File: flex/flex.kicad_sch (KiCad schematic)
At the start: 139 parts, among them J1 NA_Conn_01x06_Female, J2 NA_Conn_01x05_Female, J3 NA_Conn_01x06_Female, J4 NA_Conn_01x03_Female, J5 NA_Conn_01x03_Female, SW1 SW_Push, SW10 SW_Push, SW11 SW_Push, SW12 SW_Push, SW13 SW_Push, SW14 SW_Push, SW15 SW_Push, SW16 SW_Push, SW17 SW_Push, SW18 SW_Push, SW19 SW_Push, SW2 SW_Push, SW20 SW_Push, SW21 SW_Push, SW22 SW_Push, SW23 SW_Push, SW24 SW_Push, SW3 SW_Push, SW4 SW_Push, SW5 SW_Push, SW6 SW_Push, SW7 SW_Push, SW8 SW_Push, SW9 SW_Push

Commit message: BOM
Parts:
- added C4, C5: C, libs:C_0603_1608Metric, symbol Device:C
- added R4, R5: R, libs:R_0603_1608Metric, symbol Device:R
- C3, J1, J2, J3, J4, J5, Mousebite1, Mousebite10, Mousebite11, Mousebite12, Mousebite2, Mousebite3, Mousebite4, Mousebite5, Mousebite6, Mousebite7, Mousebite8, Mousebite9, R3, SW1, SW10, SW11, SW12, SW13, SW14, SW15, SW16, SW17, SW18, SW19, SW2, SW20, SW21, SW22, SW23, SW24, SW3, SW4, SW5, SW6, SW7, SW8, SW9: now not fitted
- D1, D10, D11, D12, D2, D25, D26, D27, D28, D29, D3, D30, D31, D32, D33, D34, D35, D36, D4, D49, D5, D50, D51, D52, D53, D54, D55, D56, D57, D58, D59, D6, D60, D61, D62, D63, D64, D65, D66, D67, D68, D69, D7, D70, D71, D72, D8, D9: LCSC (none) -> C81598
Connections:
- net Din: now also R4.1, R5.1
- net Gnd: now also C4.2, C5.2
- net Vcc: now also C4.1, C5.1
- net at D13.3 (DIN), D97.3 (DIN), R3.2: now also R4.2, R5.2

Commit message: BOM
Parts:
- D100, D101, D102, D103, D104, D105, D106, D107, D108, D109, D110, D111, D112, D113, D114, D115, D116, D117, D118, D119, D120, D13, D14, D15, D16, D17, D18, D19, D20, D21, D22, D23, D24, D37, D38, D39, D40, D41, D42, D43, D44, D45, D46, D47, D48, D97, D98, D99: LCSC C2890035 -> C5149201
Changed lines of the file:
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@@
 			)
 		)
-		(property "LCSC" "C2890035"
+		(property "LCSC" "C5149201"
 			(at 148.59 204.47 0)
 			(effects
@@
 			)
 		)
-		(property "LCSC" "C2890035"
+		(property "LCSC" "C5149201"
 			(at 193.04 204.47 0)
 			(effects
@@
 			)
 		)
-		(property "LCSC" "C2890035"
+		(property "LCSC" "C5149201"
 			(at 267.97 127 0)
 			(effects
@@
 			)
 		)
-		(property "LCSC" "C2890035"
+		(property "LCSC" "C5149201"
 			(at 148.59 186.69 0)
 			(effects
@@
 			)
 		)
-		(property "LCSC" "C2890035"
+		(property "LCSC" "C5149201"
 			(at 81.28 127 0)
 			(effects
@@
 			)
 		)
-		(property "LCSC" "C2890035"
+		(property "LCSC" "C5149201"
 			(at 312.42 127 0)
 			(effects
@@
 			)
 		)
-		(property "LCSC" "C2890035"
+		(property "LCSC" "C5149201"
 			(at 289.56 146.05 0)
 			(effects
@@
 			)
 		)
-		(property "LCSC" "C2890035"
+		(property "LCSC" "C5149201"
 			(at 223.52 127 0)
 			(effects
@@
 			)
 		)
-		(property "LCSC" "C2890035"
+		(property "LCSC" "C5149201"
 			(at 82.55 186.69 0)
 			(effects
@@
 			)
 		)
-		(property "LCSC" "C2890035"
+		(property "LCSC" "C5149201"
 			(at 104.14 186.69 0)
 			(effects
@@
 			)
 		)
-		(property "LCSC" "C2890035"
+		(property "LCSC" "C5149201"
 			(at 289.56 127 0)
 			(effects
@@
 			)
 		)
-		(property "LCSC" "C2890035"
+		(property "LCSC" "C5149201"
 			(at 312.42 146.05 0)
 			(effects
@@
 			)
 		)
-		(property "LCSC" "C2890035"
+		(property "LCSC" "C5149201"
 			(at 127 186.69 0)
 			(effects
@@
 			)
 		)
-		(property "LCSC" "C2890035"
+		(property "LCSC" "C5149201"
 			(at 193.04 186.69 0)
 			(effects
@@
 			)
 		)
-		(property "LCSC" "C2890035"
+		(property "LCSC" "C5149201"
 			(at 245.11 146.05 0)
 			(effects
@@
 			)
 		)
-		(property "LCSC" "C2890035"
+		(property "LCSC" "C5149201"
 			(at 127 204.47 0)
 			(effects
@@
 			)
 		)
-		(property "LCSC" "C2890035"
+		(property "LCSC" "C5149201"
 			(at 81.28 146.05 0)
 			(effects
@@
 			)
 		)
-		(property "LCSC" "C2890035"
+		(property "LCSC" "C5149201"
 			(at 326.39 186.69 0)
 			(effects
@@
 			)
 		)
-		(property "LCSC" "C2890035"
+		(property "LCSC" "C5149201"
 			(at 334.01 146.05 0)
 			(effects
@@
 			)
 		)
-		(property "LCSC" "C2890035"
+		(property "LCSC" "C5149201"
 			(at 281.94 204.47 0)
 			(effects
@@
 			)
 		)
-		(property "LCSC" "C2890035"
+		(property "LCSC" "C5149201"
 			(at 104.14 146.05 0)
 			(effects
@@
 			)
 		)
-		(property "LCSC" "C2890035"
+		(property "LCSC" "C5149201"
 			(at 179.07 127 0)
 			(effects
@@
 			)
 		)
-		(property "LCSC" "C2890035"
+		(property "LCSC" "C5149201"
 			(at 215.9 204.47 0)
 			(effects
@@
 			)
 		)
-		(property "LCSC" "C2890035"
+		(property "LCSC" "C5149201"
 			(at 200.66 127 0)
 			(effects
@@
 			)
 		)
-		(property "LCSC" "C2890035"
+		(property "LCSC" "C5149201"
 			(at 223.52 146.05 0)
 			(effects
@@
 			)
 		)
-		(property "LCSC" "C2890035"
+		(property "LCSC" "C5149201"
 			(at 200.66 146.05 0)
 			(effects
@@
 			)
 		)
-		(property "LCSC" "C2890035"
+		(property "LCSC" "C5149201"
 			(at 260.35 186.69 0)
 			(effects
@@
 			)
 		)
-		(property "LCSC" "C2890035"
+		(property "LCSC" "C5149201"
 			(at 304.8 186.69 0)
 			(effects
@@
 			)
 		)
-		(property "LCSC" "C2890035"
+		(property "LCSC" "C5149201"
 			(at 260.35 204.47 0)
 			(effects
@@
 			)
 		)
-		(property "LCSC" "C2890035"
+		(property "LCSC" "C5149201"
 			(at 237.49 204.47 0)
 			(effects
@@
 			)
 		)
-		(property "LCSC" "C2890035"
+		(property "LCSC" "C5149201"
 			(at 334.01 127 0)
 			(effects
@@
 			)
 		)
-		(property "LCSC" "C2890035"
+		(property "LCSC" "C5149201"
 			(at 171.45 204.47 0)
 			(effects
@@
 			)
 		)
-		(property "LCSC" "C2890035"
+		(property "LCSC" "C5149201"
 			(at 104.14 204.47 0)
 			(effects
@@
 			)
 		)
-		(property "LCSC" "C2890035"
+		(property "LCSC" "C5149201"
 			(at 215.9 186.69 0)
 			(effects
@@
 			)
 		)
-		(property "LCSC" "C2890035"
+		(property "LCSC" "C5149201"
 			(at 82.55 204.47 0)
 			(effects
@@
 			)
 		)
-		(property "LCSC" "C2890035"
+		(property "LCSC" "C5149201"
 			(at 179.07 146.05 0)
 			(effects
@@
 			)
 		)
-		(property "LCSC" "C2890035"
+		(property "LCSC" "C5149201"
 			(at 171.45 186.69 0)
 			(effects
@@
 			)
 		)
-		(property "LCSC" "C2890035"
+		(property "LCSC" "C5149201"
 			(at 125.73 127 0)
 			(effects
@@
 			)
 		)
-		(property "LCSC" "C2890035"
+		(property "LCSC" "C5149201"
 			(at 326.39 204.47 0)
 			(effects
@@
 			)
 		)
-		(property "LCSC" "C2890035"
+		(property "LCSC" "C5149201"
 			(at 148.59 127 0)
 			(effects
@@
 			)
 		)
-		(property "LCSC" "C2890035"
+		(property "LCSC" "C5149201"
 			(at 304.8 204.47 0)
 			(effects
@@
 			)
 		)
-		(property "LCSC" "C2890035"
+		(property "LCSC" "C5149201"
 			(at 245.11 127 0)
 			(effects
@@
 			)
 		)
-		(property "LCSC" "C2890035"
+		(property "LCSC" "C5149201"
 			(at 104.14 127 0)
 			(effects
@@
 			)
 		)
-		(property "LCSC" "C2890035"
+		(property "LCSC" "C5149201"
 			(at 281.94 186.69 0)
 			(effects
@@
 			)
 		)
-		(property "LCSC" "C2890035"
+		(property "LCSC" "C5149201"
 			(at 237.49 186.69 0)
 			(effects
@@
 			)
 		)
-		(property "LCSC" "C2890035"
+		(property "LCSC" "C5149201"
 			(at 125.73 146.05 0)
 			(effects
@@
 			)
 		)
-		(property "LCSC" "C2890035"
+		(property "LCSC" "C5149201"
 			(at 267.97 146.05 0)
 			(effects
@@
 			)
 		)
-		(property "LCSC" "C2890035"
+		(property "LCSC" "C5149201"
 			(at 148.59 146.05 0)
 			(effects

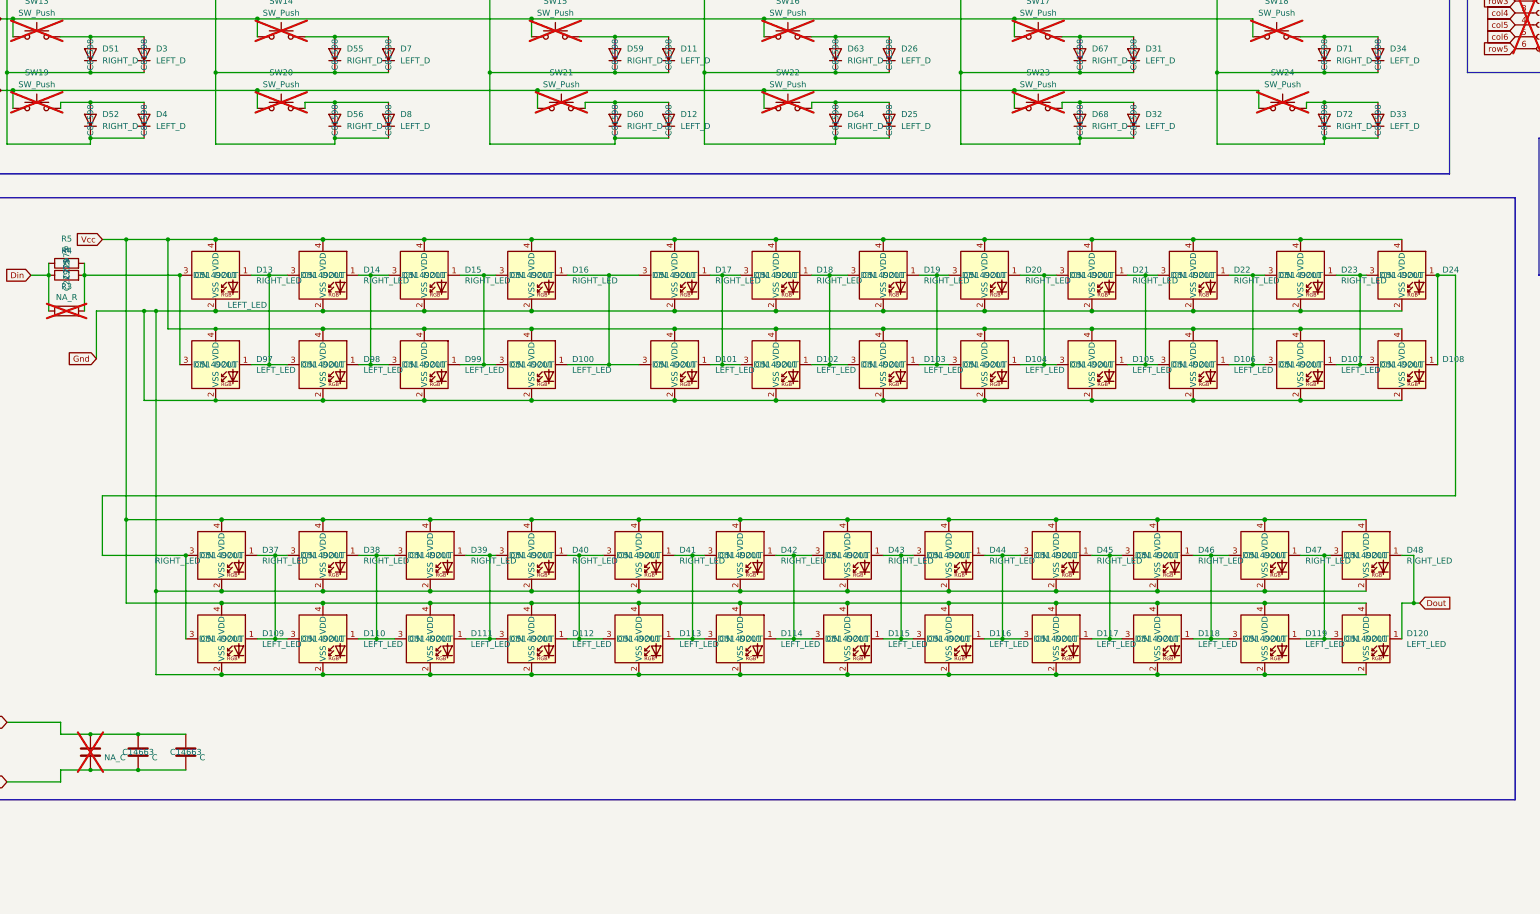
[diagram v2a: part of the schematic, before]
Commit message: place vcc pads
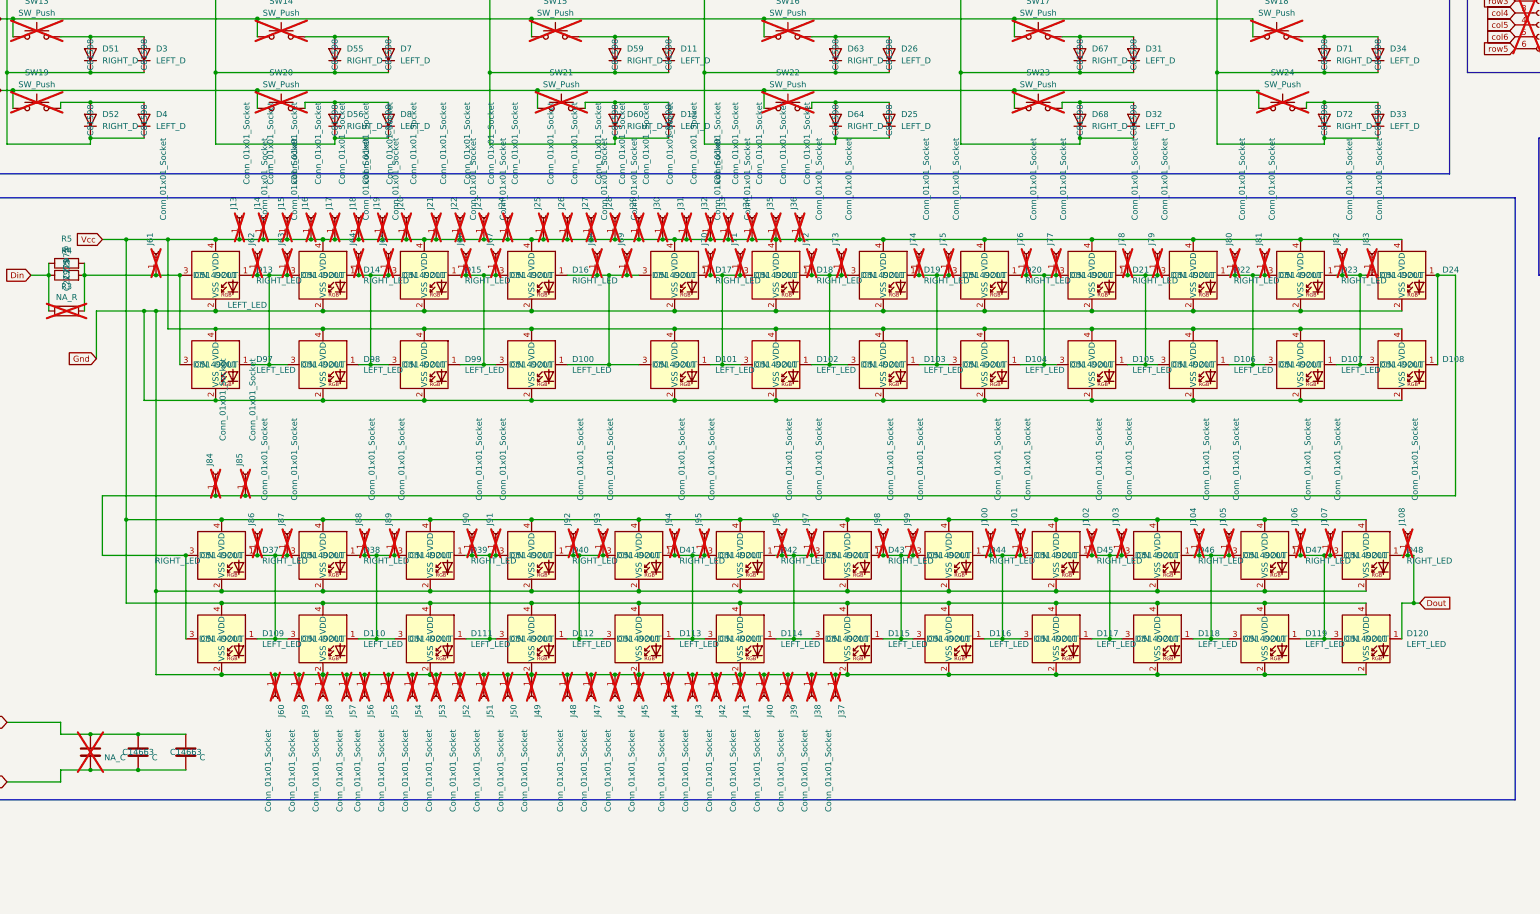
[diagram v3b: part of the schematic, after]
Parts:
- added J100, J101, J102, J103, J104, J105, J106, J107, J108, J13, J14, J15, J16, J17, J18, J19, J20, J21, J22, J23, J24, J25, J26, J27, J28, J29, J30, J31, J32, J33, J34, J35, J36, J37, J38, J39, J40, J41, J42, J43, J44, J45, J46, J47, J48, J49, J50, J51, J52, J53, J54, J55, J56, J57, J58, J59, J60, J61, J62, J63, J64, J65, J66, J67, J68, J69, J70, J71, J72, J73, J74, J75, J76, J77, J78, J79, J80, J81, J82, J83, J84, J85, J86, J87, J88, J89, J90, J91, J92, J93, J94, J95, J96, J97, J98, J99: Conn_01x01_Socket, local-libraries:PinHeader_1x01_P1.27mm_Vertical, symbol Connector:Conn_01x01_Socket
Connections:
- net Dout: now also J108.1 (Pin_1)
- net Gnd: now also J37.1 (Pin_1), J38.1 (Pin_1), J39.1 (Pin_1), J40.1 (Pin_1), J41.1 (Pin_1), J42.1 (Pin_1), J43.1 (Pin_1), J44.1 (Pin_1), J45.1 (Pin_1), J46.1 (Pin_1), J47.1 (Pin_1), J48.1 (Pin_1), J49.1 (Pin_1), J50.1 (Pin_1), J51.1 (Pin_1), J52.1 (Pin_1), J53.1 (Pin_1), J54.1 (Pin_1), J55.1 (Pin_1), J56.1 (Pin_1), J57.1 (Pin_1), J58.1 (Pin_1), J59.1 (Pin_1), J60.1 (Pin_1)
- net Vcc: now also J13.1 (Pin_1), J14.1 (Pin_1), J15.1 (Pin_1), J16.1 (Pin_1), J17.1 (Pin_1), J18.1 (Pin_1), J19.1 (Pin_1), J20.1 (Pin_1), J21.1 (Pin_1), J22.1 (Pin_1), J23.1 (Pin_1), J24.1 (Pin_1), J25.1 (Pin_1), J26.1 (Pin_1), J27.1 (Pin_1), J28.1 (Pin_1), J29.1 (Pin_1), J30.1 (Pin_1), J31.1 (Pin_1), J32.1 (Pin_1), J33.1 (Pin_1), J34.1 (Pin_1), J35.1 (Pin_1), J36.1 (Pin_1)
- net at D112.1 (DOUT), D113.3 (DIN), D40.1 (DOUT)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: now also J92.1 (Pin_1), J93.1 (Pin_1)
- net at D111.1 (DOUT), D112.3 (DIN), D39.1 (DOUT)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: now also J90.1 (Pin_1), J91.1 (Pin_1)
- net at D114.1 (DOUT), D115.3 (DIN), D42.1 (DOUT)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: now also J96.1 (Pin_1), J97.1 (Pin_1)
- net at D113.1 (DOUT), D114.3 (DIN), D41.1 (DOUT)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: now also J94.1 (Pin_1), J95.1 (Pin_1)
- net at D105.1 (DOUT), D106.3 (DIN), D21.1 (DOUT)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: now also J78.1 (Pin_1), J79.1 (Pin_1)
- net at D104.1 (DOUT), D105.3 (DIN), D20.1 (DOUT)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: now also J76.1 (Pin_1), J77.1 (Pin_1)
- net at D13.1 (DOUT), D14.3 (DIN), D97.1 (DOUT)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: now also J62.1 (Pin_1), J63.1 (Pin_1)
- net at D13.3 (DIN), D97.3 (DIN), R3.2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: now also J61.1 (Pin_1)
- net at D107.1 (DOUT), D108.3 (DIN), D23.1 (DOUT)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: now also J82.1 (Pin_1)
- net at D106.1 (DOUT), D107.3 (DIN), D22.1 (DOUT)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: now also J80.1 (Pin_1), J81.1 (Pin_1)
- net at D103.1 (DOUT), D104.3 (DIN), D19.1 (DOUT)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: now also J74.1 (Pin_1), J75.1 (Pin_1)
- net at D102.1 (DOUT), D103.3 (DIN), D18.1 (DOUT)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: now also J72.1 (Pin_1), J73.1 (Pin_1)
- net at D109.1 (DOUT), D110.3 (DIN), D37.1 (DOUT)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: now also J86.1 (Pin_1), J87.1 (Pin_1)
- net at D108.1 (DOUT), D109.3 (DIN), D24.1 (DOUT)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: now also J84.1 (Pin_1), J85.1 (Pin_1)
- net at D110.1 (DOUT), D111.3 (DIN), D38.1 (DOUT)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: now also J88.1 (Pin_1), J89.1 (Pin_1)
- net at D119.1 (DOUT), D120.3 (DIN), D47.1 (DOUT)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: now also J106.1 (Pin_1), J107.1 (Pin_1)
- net at D118.1 (DOUT), D119.3 (DIN), D46.1 (DOUT)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: now also J104.1 (Pin_1), J105.1 (Pin_1)
- net at D117.1 (DOUT), D118.3 (DIN), D45.1 (DOUT)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: now also J102.1 (Pin_1), J103.1 (Pin_1)
- net at D14.1 (DOUT), D15.3 (DIN), D98.1 (DOUT)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: now also J64.1 (Pin_1), J65.1 (Pin_1)
- net at D101.1 (DOUT), D102.3 (DIN), D17.1 (DOUT)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: now also J70.1 (Pin_1), J71.1 (Pin_1)
- net at D100.1 (DOUT), D101.3 (DIN), D16.1 (DOUT)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: now also J68.1 (Pin_1), J69.1 (Pin_1)
- net at D115.1 (DOUT), D116.3 (DIN), D43.1 (DOUT)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: now also J98.1 (Pin_1), J99.1 (Pin_1)
- net at D116.1 (DOUT), D117.3 (DIN), D44.1 (DOUT)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: now also J100.1 (Pin_1), J101.1 (Pin_1)
- net at D100.3 (DIN), D15.1 (DOUT), D16.3 (DIN)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: now also J66.1 (Pin_1), J67.1 (Pin_1)

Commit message: Update flex.kicad_sch
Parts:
- J100, J101, J102, J103, J104, J105, J106, J107, J108, J13, J14, J15, J16, J17, J18, J19, J20, J21, J22, J23, J24, J25, J26, J27, J28, J29, J30, J31, J32, J33, J34, J35, J36, J37, J38, J39, J40, J41, J42, J43, J44, J45, J46, J47, J48, J49, J50, J51, J52, J53, J54, J55, J56, J57, J58, J59, J60, J61, J62, J63, J64, J65, J66, J67, J68, J69, J70, J71, J72, J73, J74, J75, J76, J77, J78, J79, J80, J81, J82, J83, J84, J85, J86, J87, J88, J89, J90, J91, J92, J93, J94, J95, J96, J97, J98, J99: footprint local-libraries:PinHeader_1x01_P1.27mm_Vertical -> custom:PinHeader_1x01_P1.27mm_Vertical

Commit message: silkscreen
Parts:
- added J109, J110, J111, J112, J113, J114, J115: Conn_01x01_Socket, custom:PinHeader_1x01_P1.27mm_Vertical, symbol Connector:Conn_01x01_Socket
- J100, J102, J104, J106, J108, J62, J64, J66, J68, J70, J72, J74, J76, J78, J80, J82, J85, J86, J88, J90, J92, J94, J96, J98: footprint custom:PinHeader_1x01_P1.27mm_Vertical -> custom:PinHeader_1x01_P1.27mm_Vertical_OUT
- J101, J103, J105, J107, J61, J63, J65, J67, J69, J71, J73, J75, J77, J79, J81, J83, J84, J87, J89, J91, J93, J95, J97, J99: footprint custom:PinHeader_1x01_P1.27mm_Vertical -> custom:PinHeader_1x01_P1.27mm_Vertical_IN
- J13, J14, J15, J16, J17, J18, J19, J20, J21, J22, J23, J24, J25, J26, J27, J28, J29, J30, J31, J32, J33, J34, J35, J36: footprint custom:PinHeader_1x01_P1.27mm_Vertical -> custom:PinHeader_1x01_P1.27mm_Vertical_VCC
- J37, J38, J39, J40, J41, J42, J43, J44, J45, J46, J47, J48, J49, J50, J51, J52, J53, J54, J55, J56, J57, J58, J59, J60: footprint custom:PinHeader_1x01_P1.27mm_Vertical -> custom:PinHeader_1x01_P1.27mm_Vertical_GND
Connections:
- net col1: now also J109.1 (Pin_1), J115.1 (Pin_1)
- net col2: now also J110.1 (Pin_1)
- net col3: now also J111.1 (Pin_1)
- net col4: now also J112.1 (Pin_1)
- net col5: now also J113.1 (Pin_1)
- net col6: now also J114.1 (Pin_1)

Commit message: DRC, silkscreen
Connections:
- net at D107.1 (DOUT), D108.3 (DIN), D23.1 (DOUT)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: now also J83.1 (Pin_1)
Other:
- moved on the sheet: J83
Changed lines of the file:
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@@
 	)
 	(junction
+		(at 326.39 127)
+		(diameter 0)
+		(color 0 0 0 0)
+	)
+	(junction
 		(at 318.77 186.69)
 		(diameter 0)
@@
 	(symbol
 		(lib_id "Connector:Conn_01x01_Socket")
-		(at 327.66 121.92 90)
+		(at 326.39 121.92 90)
 		(unit 1)
 		(exclude_from_sim no)
@@
 		(dnp yes)
 		(property "Reference" "J83"
-			(at 326.3899 120.65 0)
+			(at 325.1199 120.65 0)
 			(effects
 				(font
@@
 		)
 		(property "Value" "Conn_01x01_Socket"
-			(at 329.184 115.316 0)
+			(at 327.914 115.316 0)
 			(effects
 				(font
@@
 		)
 		(property "Footprint" "custom:PinHeader_1x01_P1.27mm_Vertical_IN"
-			(at 327.66 121.92 0)
+			(at 326.39 121.92 0)
 			(effects
 				(font
@@
 		)
 		(property "Datasheet" "~"
-			(at 327.66 121.92 0)
+			(at 326.39 121.92 0)
 			(effects
 				(font
@@
 		)
 		(property "Description" "Generic connector, single row, 01x01, script generated"
-			(at 327.66 121.92 0)
+			(at 326.39 121.92 0)
 			(effects
 				(font
